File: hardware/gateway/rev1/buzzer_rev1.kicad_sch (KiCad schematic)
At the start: 16 parts, among them IC3 LT1615ES5-1#TRMPBF, IC4 MIC4427YM

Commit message: Replaced 0402  by 0603 package where was possible.
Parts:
- R15: footprint Resistor_SMD:R_0402_1005Metric -> Resistor_SMD:R_0603_1608Metric; Manufacturer Yageo -> Vishay; Manufacturer Part Number RC0402JR-7D100KL -> MCT06030C1003FP5; Mouser Part Number 603-RC0402JR-7D100KL -> 594-MCT06030C1003FP5; Supplier Link https://pt.mouser.com/ProductDetail/YAGEO/RC0402JR-7D100KL?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 -> https://pt.mouser.com/ProductDetail/Vishay-Beyschlag/MCT060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
- R18, R19: footprint Resistor_SMD:R_0402_1005Metric -> Resistor_SMD:R_0603_1608Metric; Manufacturer Panasonic -> Yageo; Manufacturer Part Number ERJ-S02J330X -> SR0603JR-7T33RL; Mouser Part Number 667-ERJ-S02J330X -> 603-SR0603JR-7T33RL; Supplier Link https://pt.mouser.com/ProductDetail/Panasonic/ERJ-S02J330X?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 -> https://pt.mouser.com/ProductDetail/YAGEO/SR0603JR-7T33RL?q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
- R20: footprint Resistor_SMD:R_0402_1005Metric -> Resistor_SMD:R_0603_1608Metric; Manufacturer Panasonic -> Yageo; Manufacturer Part Number ERJ-2RKD1004X -> AR0603FR-071ML; Mouser Part Number 667-ERJ-2RKD1004X -> 603-AR0603FR-071ML; Supplier Link https://pt.mouser.com/ProductDetail/Panasonic/ERJ-2RKD1004X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 -> https://pt.mouser.com/ProductDetail/YAGEO/AR0603FR-071ML?qs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
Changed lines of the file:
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@@
 			)
 		)
-		(property "Footprint" "Resistor_SMD:R_0402_1005Metric"
+		(property "Footprint" "Resistor_SMD:R_0603_1608Metric"
 			(at 103.886 99.314 90)
 			(effects
@@
 			)
 		)
-		(property "Mouser Part Number" "667-ERJ-S02J330X"
+		(property "Mouser Part Number" "603-SR0603JR-7T33RL"
 			(at 104.14 100.33 0)
 			(effects
@@
 			)
 		)
-		(property "Supplier Link" "https://pt.mouser.com/ProductDetail/Panasonic/ERJ-S02J330X?qs=sGAEpiMZZMvdGkrng054t%252BB3dTvXmYJZ97y%2FhHbL7G0%3D"
+		(property "Supplier Link" "https://pt.mouser.com/ProductDetail/YAGEO/SR0603JR-7T33RL?qs=1mbolxNpo8eV8es9T7q7Sg%3D%3D"
 			(at 104.14 100.33 0)
 			(effects
@@
 			)
 		)
-		(property "Manufacturer" "Panasonic"
+		(property "Manufacturer" "Yageo"
 			(at 104.14 100.33 0)
 			(effects
@@
 			)
 		)
-		(property "Manufacturer Part Number" "ERJ-S02J330X"
+		(property "Manufacturer Part Number" "SR0603JR-7T33RL"
 			(at 104.14 100.33 0)
 			(effects
@@
 			)
 		)
-		(property "Footprint" "Resistor_SMD:R_0402_1005Metric"
+		(property "Footprint" "Resistor_SMD:R_0603_1608Metric"
 			(at 103.886 96.266 90)
 			(effects
@@
 			)
 		)
-		(property "Mouser Part Number" "667-ERJ-S02J330X"
+		(property "Mouser Part Number" "603-SR0603JR-7T33RL "
 			(at 104.14 95.25 0)
 			(effects
@@
 			)
 		)
-		(property "Supplier Link" "https://pt.mouser.com/ProductDetail/Panasonic/ERJ-S02J330X?qs=sGAEpiMZZMvdGkrng054t%252BB3dTvXmYJZ97y%2FhHbL7G0%3D"
+		(property "Supplier Link" "https://pt.mouser.com/ProductDetail/YAGEO/SR0603JR-7T33RL?qs=1mbolxNpo8eV8es9T7q7Sg%3D%3D"
 			(at 104.14 95.25 0)
 			(effects
@@
 			)
 		)
-		(property "Manufacturer" "Panasonic"
+		(property "Manufacturer" "Yageo"
 			(at 104.14 95.25 0)
 			(effects
@@
 			)
 		)
-		(property "Manufacturer Part Number" "ERJ-S02J330X"
+		(property "Manufacturer Part Number" "SR0603JR-7T33RL "
 			(at 104.14 95.25 0)
 			(effects
@@
 			)
 		)
-		(property "Footprint" "Resistor_SMD:R_0402_1005Metric"
+		(property "Footprint" "Resistor_SMD:R_0603_1608Metric"
 			(at 30.734 49.276 90)
 			(effects
@@
 			)
 		)
-		(property "Mouser Part Number" "603-RC0402JR-7D100KL"
+		(property "Mouser Part Number" "594-MCT06030C1003FP5"
 			(at 31.75 49.53 0)
 			(effects
@@
 			)
 		)
-		(property "Supplier Link" "https://pt.mouser.com/ProductDetail/YAGEO/RC0402JR-7D100KL?qs=sGAEpiMZZMvdGkrng054tz1y1XEHv7sNDqn1Y%252B6zGYVTl0poVAV1uA%3D%3D"
+		(property "Supplier Link" "https://pt.mouser.com/ProductDetail/Vishay-Beyschlag/MCT06030C1003FP500?qs=sGAEpiMZZMvdGkrng054typNwhVi1mc8Rk09XKJvPxA%3D"
 			(at 31.75 49.53 0)
 			(effects
@@
 			)
 		)
-		(property "Manufacturer" "Yageo"
+		(property "Manufacturer" "Vishay"
 			(at 31.75 49.53 0)
 			(effects
@@
 			)
 		)
-		(property "Manufacturer Part Number" "RC0402JR-7D100KL"
+		(property "Manufacturer Part Number" "MCT06030C1003FP5"
 			(at 31.75 49.53 0)
 			(effects
@@
 			)
 		)
-		(property "Footprint" "Resistor_SMD:R_0402_1005Metric"
+		(property "Footprint" "Resistor_SMD:R_0603_1608Metric"
 			(at 122.174 97.536 90)
 			(effects
@@
 			)
 		)
-		(property "Mouser Part Number" "667-ERJ-2RKD1004X"
+		(property "Mouser Part Number" "603-AR0603FR-071ML"
 			(at 123.19 97.79 0)
 			(effects
@@
 			)
 		)
-		(property "Supplier Link" "https://pt.mouser.com/ProductDetail/Panasonic/ERJ-2RKD1004X?qs=Ywefl8B65e6r4yb6mm%252BtoQ%3D%3D"
+		(property "Supplier Link" "https://pt.mouser.com/ProductDetail/YAGEO/AR0603FR-071ML?qs=tggtontpCXN3Ykm7Gt7Sqw%3D%3D"
 			(at 123.19 97.79 0)
 			(effects
@@
 			)
 		)
-		(property "Manufacturer" "Panasonic"
+		(property "Manufacturer" "Yageo"
 			(at 123.19 97.79 0)
 			(effects
@@
 			)
 		)
-		(property "Manufacturer Part Number" "ERJ-2RKD1004X"
+		(property "Manufacturer Part Number" "AR0603FR-071ML"
 			(at 123.19 97.79 0)
 			(effects

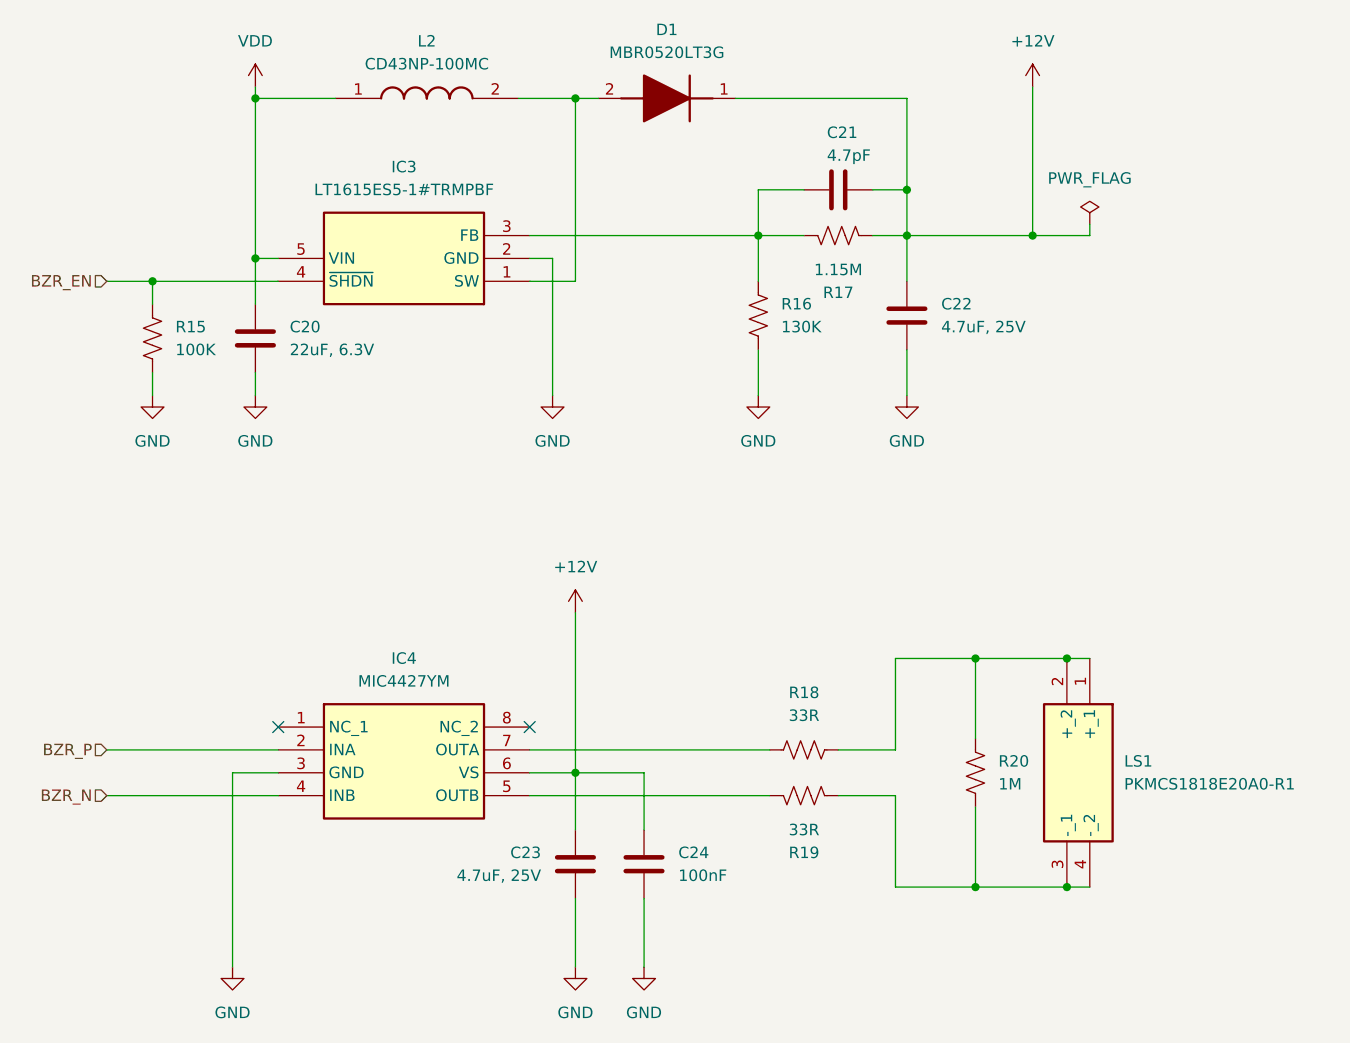
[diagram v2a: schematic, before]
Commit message: DRC errors fixed and silkscreen fixed.
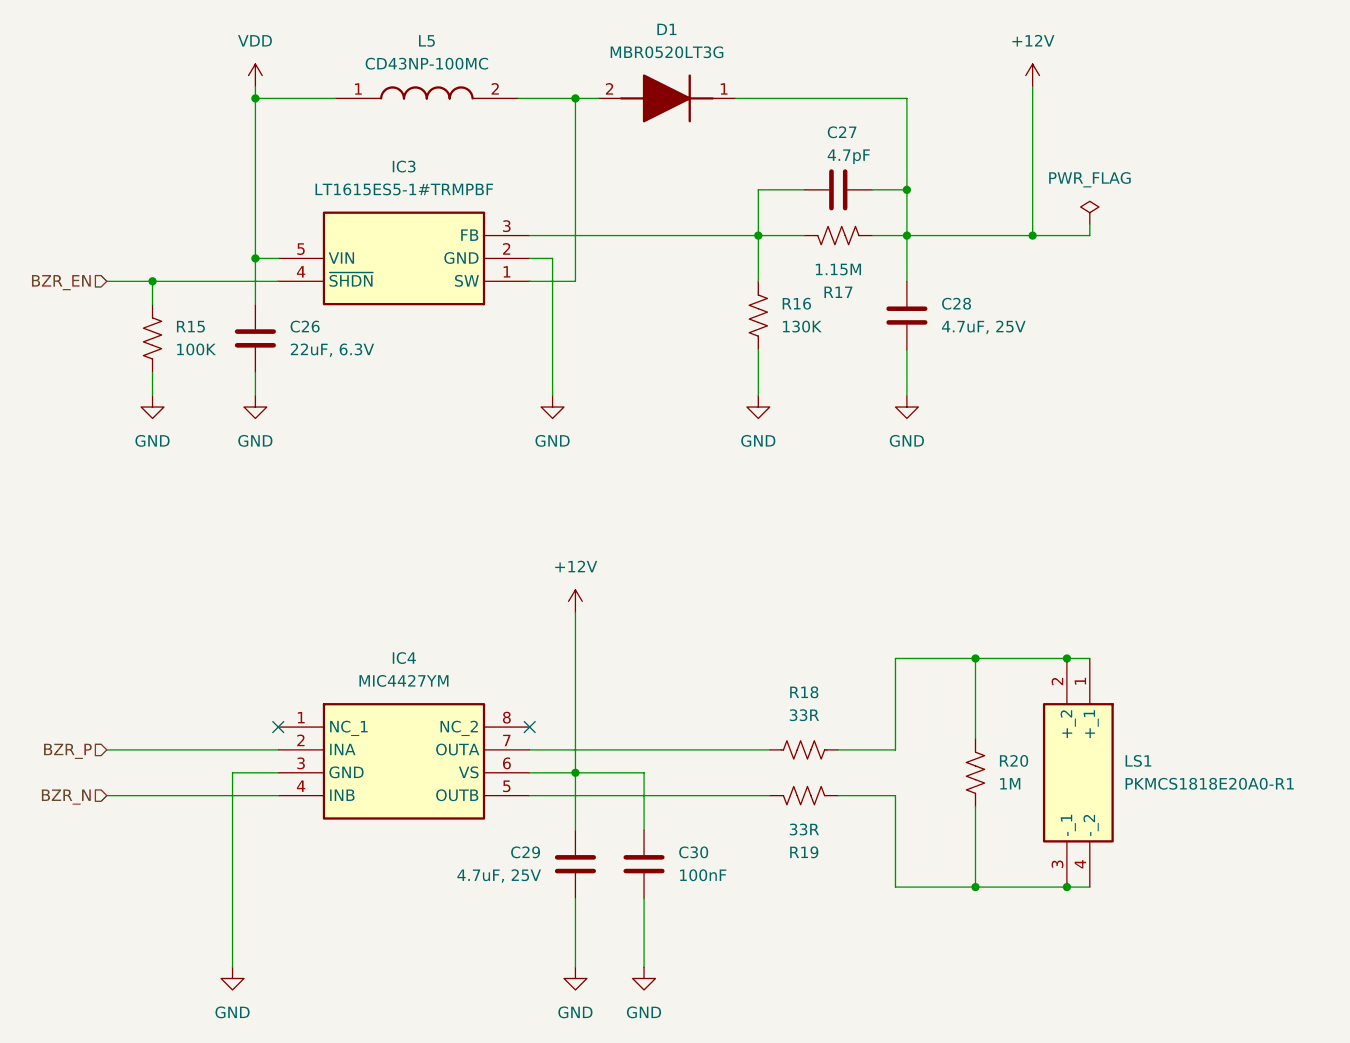
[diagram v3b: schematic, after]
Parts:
- renumbered C20 to C26, C21 to C27, C22 to C28, C23 to C29, C24 to C30, L2 to L5
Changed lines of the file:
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@@
 		(on_board yes)
 		(dnp no)
-		(property "Reference" "C23"
+		(property "Reference" "C29"
 			(at 74.93 106.6799 0)
 			(effects
@@
 			(project "gateway_rev1"
 				(path "/d3cb7130-decc-418b-958e-e5d84a8d867f/fe77db69-068b-4697-8152-e8993e362189"
-					(reference "C23")
+					(reference "C29")
 					(unit 1)
 				)
@@
 		(dnp no)
 		(fields_autoplaced yes)
-		(property "Reference" "C22"
+		(property "Reference" "C28"
 			(at 119.38 45.7199 0)
 			(effects
@@
 			(project "gateway_rev1"
 				(path "/d3cb7130-decc-418b-958e-e5d84a8d867f/fe77db69-068b-4697-8152-e8993e362189"
-					(reference "C22")
+					(reference "C28")
 					(unit 1)
 				)
@@
 		(dnp no)
 		(fields_autoplaced yes)
-		(property "Reference" "C20"
+		(property "Reference" "C26"
 			(at 46.99 48.2599 0)
 			(effects
@@
 			(project "gateway_rev1"
 				(path "/d3cb7130-decc-418b-958e-e5d84a8d867f/fe77db69-068b-4697-8152-e8993e362189"
-					(reference "C20")
+					(reference "C26")
 					(unit 1)
 				)
@@
 		(dnp no)
 		(fields_autoplaced yes)
-		(property "Reference" "L2"
+		(property "Reference" "L5"
 			(at 62.23 16.51 0)
 			(effects
@@
 			(project "gateway_rev1"
 				(path "/d3cb7130-decc-418b-958e-e5d84a8d867f/fe77db69-068b-4697-8152-e8993e362189"
-					(reference "L2")
+					(reference "L5")
 					(unit 1)
 				)
@@
 		(dnp no)
 		(fields_autoplaced yes)
-		(property "Reference" "C24"
+		(property "Reference" "C30"
 			(at 90.17 106.6799 0)
 			(effects
@@
 			(project "gateway_rev1"
 				(path "/d3cb7130-decc-418b-958e-e5d84a8d867f/fe77db69-068b-4697-8152-e8993e362189"
-					(reference "C24")
+					(reference "C30")
 					(unit 1)
 				)
@@
 		(on_board yes)
 		(dnp no)
-		(property "Reference" "C21"
+		(property "Reference" "C27"
 			(at 106.68 26.67 90)
 			(effects
@@
 			(project "gateway_rev1"
 				(path "/d3cb7130-decc-418b-958e-e5d84a8d867f/fe77db69-068b-4697-8152-e8993e362189"
-					(reference "C21")
-					(unit 1)
-				)
+					(reference "C27")
+					(unit 1)
+				)
